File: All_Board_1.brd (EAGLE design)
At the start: 109 x 69.4 mm, 105 parts, among them J1 61301611121, J2 61301611121, J3 61301611121, J4 61301611121, T1 BC817U, T10 BC817U, T11 BC817U, T12 BC817U, T13 BC817U, T14 BC817U, T2 BC817U, T3 BC817U, T7 BC817U, T8 BC817U, T9 BC817U

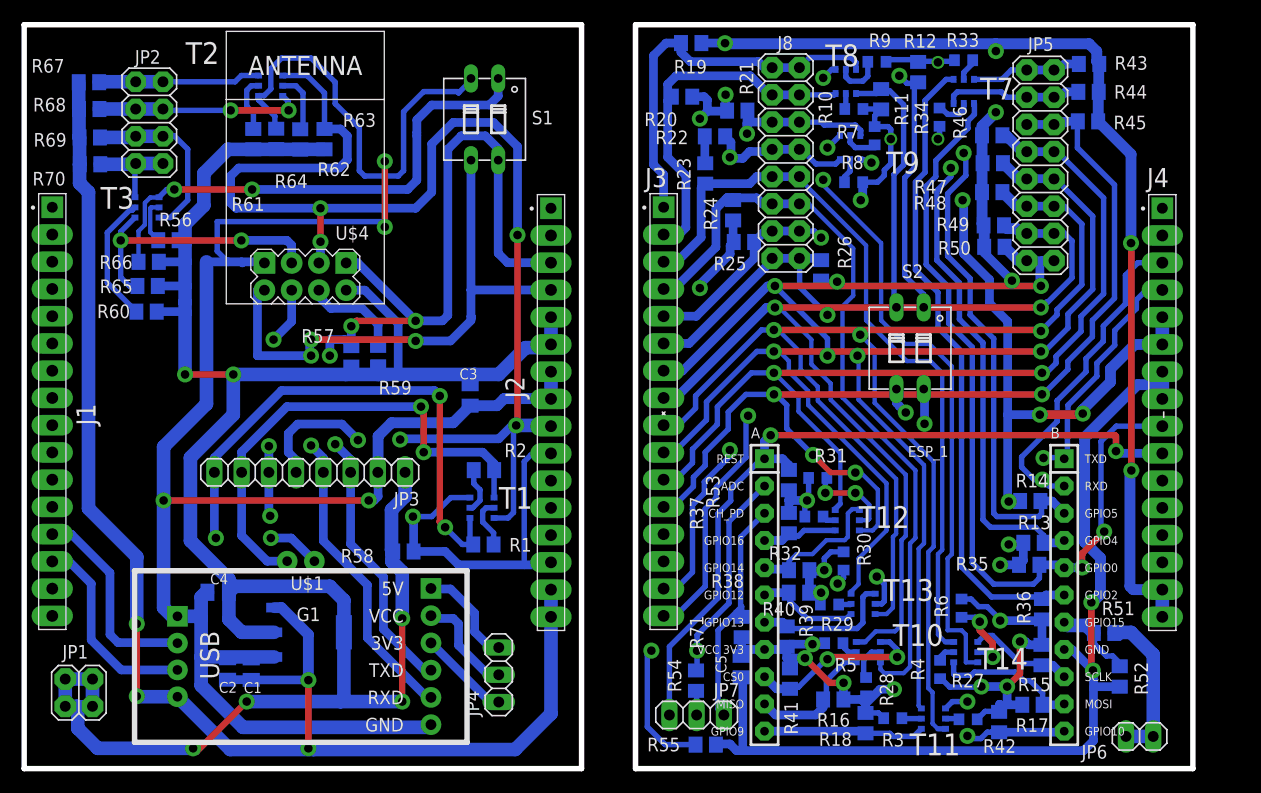
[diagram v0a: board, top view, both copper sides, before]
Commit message: zmniejszona szerokosc sciezek pod tranzystorami
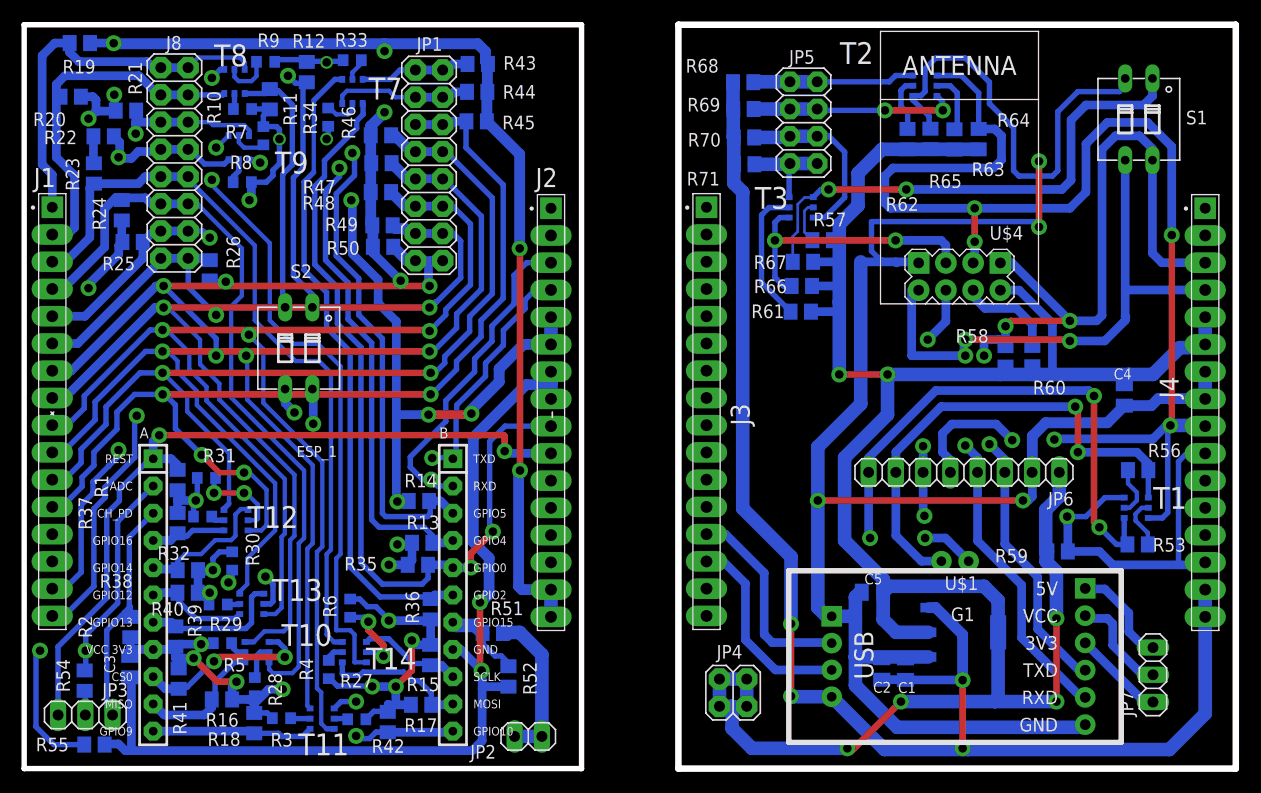
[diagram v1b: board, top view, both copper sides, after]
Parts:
- C4: value 10uF -> 100nF
- C5: value 100nF -> 10uF
- JP1: device pinhead:2X02 -> pinhead:2X08
- JP2: device pinhead:2X04 -> pinhead:1X02
- JP3: device pinhead:1X08 -> pinhead:1X03
- JP4: device pinhead:1X03 -> pinhead:2X02
- JP5: device pinhead:2X08 -> pinhead:2X04
- JP6: device pinhead:1X02 -> pinhead:1X08
- R56, R60: value 4,7K -> 10K
- R57: value 47K -> 4,7K
- R58: value 10K -> 47K
- R63: value 10K -> 4,7K
- moved R56 92.9 mm to (103.9, 27.8), turned to 180 degrees
- moved C4 86.5 mm to (102.6, 34.8), turned to 270 degrees
- moved R60 82.7 mm to (94.0, 38.5), turned to 90 degrees
- moved R65 74.3 mm to (84.5, 58.7), turned to 270 degrees
- moved R67 68.6 mm to (72.6, 47.2), turned to 180 degrees
- moved JP2 67.3 mm to (47.0, 3.00), turned to 0 degrees
- moved R59 65.9 mm to (96.4, 20.2), turned to 180 degrees
- moved R64 65.5 mm to (89.0, 58.7)
- moved R68 61.0 mm to (67.0, 64.0)
- moved R70 61.0 mm to (67.1, 58.9)
- moved R69 61.0 mm to (67.1, 61.5)
- moved S1 61.0 mm to (103.9, 60.5)
- moved U$1 61.0 mm to (86.8, 10.4)
- moved C1 61.0 mm to (82.2, 9.27)
- moved G1 61.0 mm to (87.6, 12.7)
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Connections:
- net +3V1: now also C4.1, G1.2, G1.4, JP4.1, JP4.2, JP4.3, JP4.4, JP6.1, R57.1, R58.2, R59.1, R60.1, R61.1, R62.1, R63.1, R64.2, R65.2, R66.2, R67.2, U$4.D2; no longer ESP_1.8, R10.1, R11.2, R12.2, R13.2, R14.2, R15.2, R16.2, R17.2, R18.2, R27.1, R28.1, R29.1, R3.1, R30.1, R31.1, R32.1, R33.1, R34.1, R35.2, R36.2, R37.2, R38.2, R39.2, R4.1, R40.2, R41.2, R42.2, R5.1, R53.1, R6.1, R7.1, R71.1, R8.1, R9.1
- net +3V3: now also ESP_1.8, R1.1, R10.1, R11.2, R12.2, R13.2, R14.2, R15.2, R16.2, R17.2, R18.2, R2.1, R27.1, R28.1, R29.1, R3.1, R30.1, R31.1, R32.1, R33.1, R34.1, R35.2, R36.2, R37.2, R38.2, R39.2, R4.1, R40.2, R41.2, R42.2, R5.1, R6.1, R7.1, R8.1, R9.1; no longer C4.1, G1.2, G1.4, JP1.1, JP1.2, JP1.3, JP1.4, JP3.1, R56.1, R57.2, R58.1, R59.1, R60.1, R61.1, R62.1, R63.2, R64.2, R65.2, R66.2, U$4.D2
- net +5V: now also R19.2, R20.2, R21.2, R22.2, R23.2, R24.2, R25.2, R26.2, R43.2, R44.2, R45.2, R46.2, R47.2, R48.2, R49.2, R50.2; no longer C1.1, C2.1, G1.3, R67.2, R68.2, R69.2, R70.2, U$1.PLUS
- net +5V1: now also C1.1, C2.1, G1.3, R68.2, R69.2, R70.2, R71.2, U$1.PLUS; no longer R19.2, R20.2, R21.2, R22.2, R23.2, R24.2, R25.2, R26.2, R43.2, R44.2, R45.2, R46.2, R47.2, R48.2, R49.2, R50.2
- net D+: no longer U$1.D+
- net D+1: now also U$1.D+
- net D-: no longer U$1.D-
- net D-1: now also U$1.D-
- net DTR: now also JP6.8, R53.1; no longer JP3.8, R1.1
- net ENABLE: now also ESP_1.3, JP3.1, R2.2; no longer R59.2, U$4.C2
- net ENABLE1: now also R60.2, U$4.C2; no longer ESP_1.3, JP7.1, R71.2
- net GND: now also ESP_1.16, R52.1, R55.1; no longer C1.2, C2.2, C4.2, G1.1, JP3.2, U$1.GND, U$1.MINUS, U$4.A1
- net GND1: now also C1.2, C2.2, C4.2, G1.1, JP6.2, U$1.GND, U$1.MINUS, U$4.A1; no longer ESP_1.16, R52.1, R55.1
- net GPIO0: now also ESP_1.13, R35.1, T7.1; no longer JP3.5, R63.1, T1.3, T2.1, U$4.C1
- net GPIO1: now also R11.1, S2.2, T8.1; no longer R64.1, S1.2, T2.4
- net GPIO10: now also ESP_1.22, R42.1, T11.1; no longer ESP_1.20, R15.1, T14.1
- net GPIO15: now also JP2.1, JP2.2; no longer JP6.1, JP6.2
- net GPIO17: now also J4.9, JP6.5, R64.1, T1.3, T2.1, U$4.C1; no longer ESP_1.21, R17.1, T14.4
- net GPIO18: now also R66.1, T3.1, U$4.B1; no longer ESP_1.22, R42.1, T11.1
- net GPIO19: now also R65.1, S1.2, T2.4; no longer R11.1, S2.2, T8.1
- net GPIO2: now also ESP_1.14, R36.1, T7.4; no longer R65.1, T3.1, U$4.B1
- net GPIO20: now also R67.1, S1.1, T3.4; no longer R12.1, S2.1, T8.4
- net GPIO3: now also R12.1, S2.1, T8.4; no longer R66.1, S1.1, T3.4
- net GPIO4: now also ESP_1.12, R13.1, T9.1; no longer ESP_1.13, J4.9, R35.1, T7.1
- net GPIO6: now also ESP_1.20, R15.1, T14.1; no longer ESP_1.12, R13.1, T9.1
- net GPIO8: now also ESP_1.21, R17.1, T14.4; no longer ESP_1.14, R36.1, T7.4
- net LED_A1: now also J1.9, JP1.11, JP1.12; no longer J3.9, JP5.11, JP5.12
- net LED_A2: now also J1.10, JP1.10, JP1.9; no longer J3.10, JP5.10, JP5.9
- net LED_A3: now also J1.11, JP1.7, JP1.8; no longer J3.11, JP5.7, JP5.8
- net LED_A4: now also J1.12, JP1.5, JP1.6; no longer J3.12, JP5.5, JP5.6
- net LL1: now also J1.1, J8.1, J8.2, R19.1, T8.6; no longer JP2.1, JP2.2, R67.1, T2.6
- net LL10: now also JP5.3, JP5.4, R69.1, T2.3; no longer J3.8, JP5.13, JP5.14, R49.1, T10.6
- net LL2: now also J1.2, J8.3, J8.4, R20.1, T8.3; no longer JP2.3, JP2.4, R68.1, T2.3
- net LL3: now also J1.3, J8.10, J8.9, R23.1, T14.6; no longer J3.1, J8.1, J8.2, R19.1, T8.6
- net LL4: now also J1.4, J8.11, J8.12, R24.1, T10.3; no longer J3.2, J8.3, J8.4, R20.1, T8.3
- net LL5: now also J1.5, J8.13, J8.14, R25.1, T14.3; no longer J3.3, J8.10, J8.9, R23.1, T14.6
- net LL6: now also J1.6, J8.15, J8.16, R26.1, T11.3; no longer J3.4, J8.11, J8.12, R24.1, T10.3
- net LL7: now also J1.7, JP1.15, JP1.16, R50.1, T11.6; no longer J3.5, J8.13, J8.14, R25.1, T14.3
- net LL8: now also J1.8, JP1.13, JP1.14, R49.1, T10.6; no longer J3.6, J8.15, J8.16, R26.1, T11.3
- net LL9: now also JP5.1, JP5.2, R68.1, T2.6; no longer J3.7, JP5.15, JP5.16, R50.1, T11.6
- net N$1: now also JP1.3, JP1.4, R44.1, T7.3; no longer R2.1, T1.5
- net N$10: now also JP7.3, U$1.5V; no longer JP7.2, R54.2
- net N$11: now also JP7.2; no longer JP4.2
- net N$13: now also JP7.1; no longer JP4.1
- net N$17: now also R63.2; no longer R62.2
- net N$18: now also R62.2; no longer R61.2
- net N$19: now also R61.2; no longer R60.2
- net N$2: now also JP3.2, R54.2; no longer R1.2, T1.2
- net N$21: now also R57.2; no longer R56.2
- net N$3: now also JP1.1, JP1.2; no longer JP5.1, JP5.2
- net N$5: now also R56.1, T1.5; no longer JP4.3, U$1.5V
- net N$9: now also R53.2, T1.2; no longer JP5.3, JP5.4, R44.1, T7.3
- net RESET: now also ESP_1.1, JP3.3, R1.2; no longer JP3.6, R58.2, T1.6, U$4.B2
- net RESET1: now also JP6.6, R59.2, T1.6, U$4.B2; no longer ESP_1.1, JP7.3, R53.2
- net RTS: now also JP6.7, R56.2; no longer JP3.7, R2.2
- net RXD: now also ESP_1.9, S2.3; no longer JP3.4, S1.3, U$1.RXD, U$4.A2
- net RXD1: now also JP6.4, S1.3, U$1.RXD, U$4.A2; no longer ESP_1.9, S2.3
- net SCL: now also J1.15, J8.7, J8.8, R22.1, T9.3; no longer JP2.7, JP2.8, R70.1, T3.3
- net SCL1: now also JP5.7, JP5.8, R71.1, T3.3; no longer J3.15, J8.7, J8.8, R22.1, T9.3
- net SDA: now also J1.16, J8.5, J8.6, R21.1, T9.6; no longer JP2.5, JP2.6, R69.1, T3.6
- net SDA1: now also JP5.5, JP5.6, R70.1, T3.6; no longer J3.16, J8.5, J8.6, R21.1, T9.6
- net TXD: now also ESP_1.10, S2.4; no longer JP3.3, R57.1, S1.4, U$1.TXD, U$4.D1
- net TXD1: now also JP6.3, R58.1, S1.4, U$1.TXD, U$4.D1; no longer ESP_1.10, S2.4
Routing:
- net GPIO17: track 13.5 -> 127.9 mm, vias 0 -> 6
- net LL9: track 91.5 -> 15.3 mm, vias 4 -> 0
- net LL10: track 93.1 -> 19.3 mm
- net GND1: track 89.8 -> 154.5 mm, vias 2 -> 4
- net GND: track 154.5 -> 89.8 mm, vias 4 -> 2
- net +3V1: track 157.2 -> 214.1 mm, vias 21 -> 6
- net +3V3: track 214.1 -> 158.0 mm, vias 6 -> 21
- net RXD1: track 25.8 -> 80.0 mm, vias 2 -> 4
- net RXD: track 80.0 -> 25.8 mm, vias 4 -> 2
- net TXD1: track 34.0 -> 85.6 mm, vias 2 -> 4
- net TXD: track 85.6 -> 34.0 mm, vias 4 -> 2
- net GPIO0: track 127.9 -> 78.2 mm, vias 6 -> 2
- net GPIO8: track 60.1 -> 13.5 mm
- net LL4: track 33.7 -> 73.7 mm
- net GPIO6: track 45.3 -> 9.65 mm, vias 2 -> 0
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- added copper zone on layer 16, net GND1
- removed copper zone on layer 16, net GND
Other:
- board size 109 x 69.4 mm -> 113 x 69.4 mm
